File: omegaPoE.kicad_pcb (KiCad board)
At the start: 4 copper layers, 32.4 x 48 mm, 85 parts, among them J1 RJ45-TRANS_POE, J2 CONN_EXPANSION, J3 Conn_02x01, J4 Conn_02x01, Q1 FDM3622, Q2 Q_NMOS_GSD, SW1 SW_Push, T1 PA1276, U1 LM5070, U2 PS2501-1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

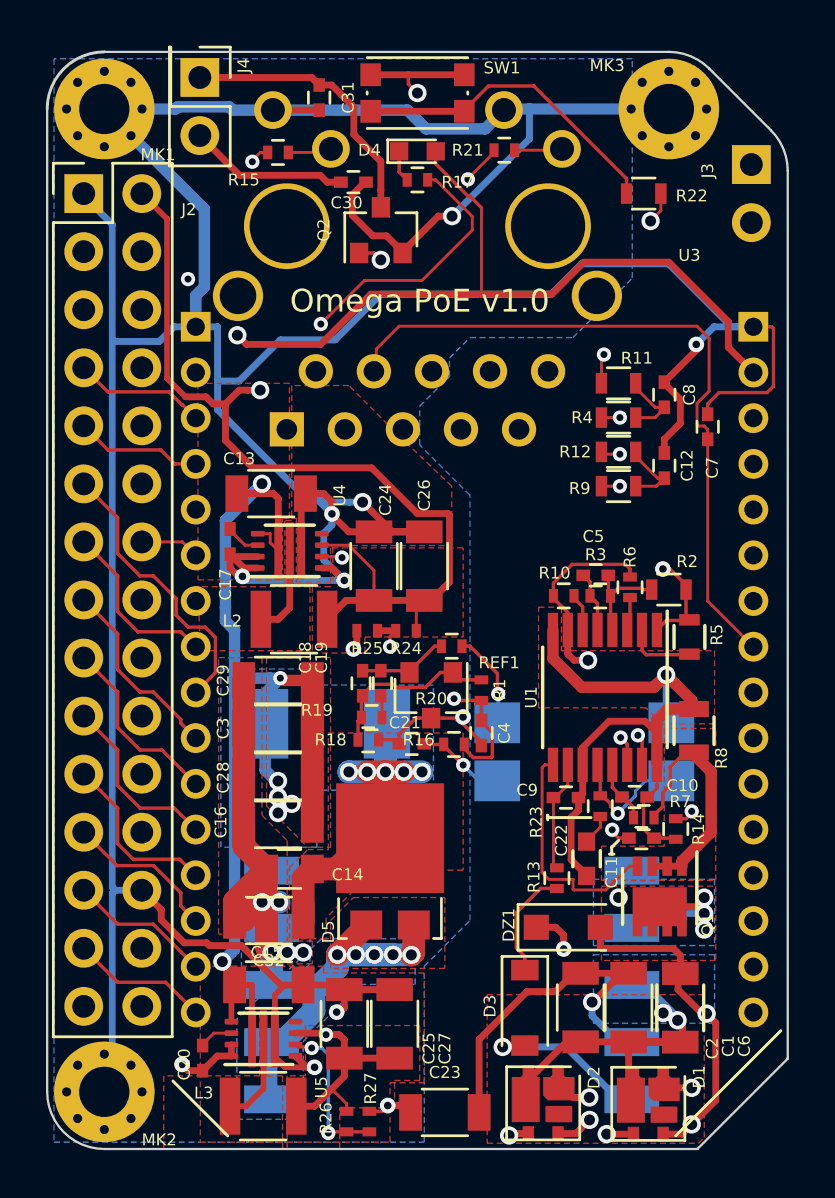
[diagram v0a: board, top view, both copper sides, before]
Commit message: Added rever-semount LED for testing, cleaned up MPN listings some more.
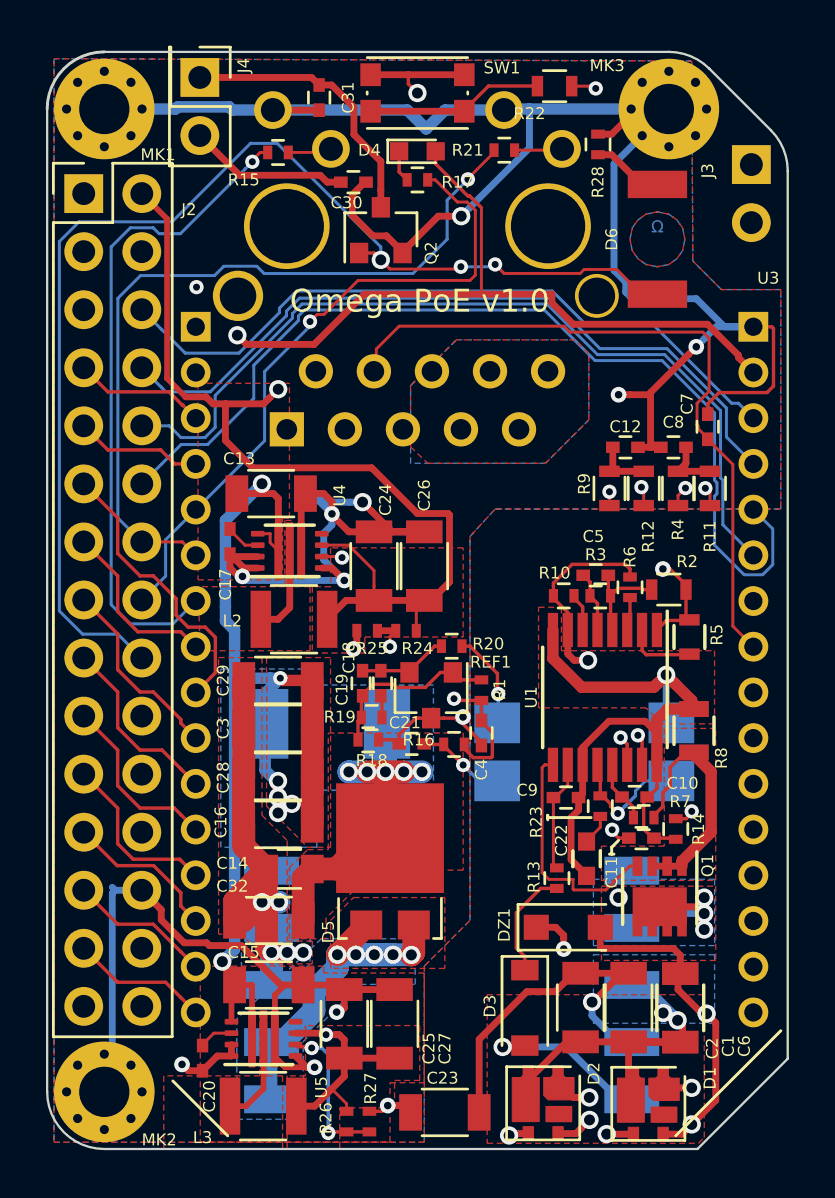
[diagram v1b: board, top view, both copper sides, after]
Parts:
- added D6: LED, lib_fp:LED_reverse_gull, F.Cu at (111.2, 59.7)
- added R28: 100, Resistors_SMD:R_0402, F.Cu at (108.6, 55.5)
- moved R22 6.11 mm to (106.7, 53.0)
- moved R11 6.10 mm to (113.5, 70.6), turned to 90 degrees
- moved R4 4.05 mm to (112.1, 70.6), turned to 270 degrees
- moved C8 2.33 mm to (111.9, 68.8), turned to 180 degrees
- moved R12 1.94 mm to (110.6, 70.6), turned to 90 degrees
- moved C12 1.88 mm to (109.8, 68.8), turned to 0 degrees
- moved R9 0.41 mm to (109.1, 70.6), turned to 270 degrees
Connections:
- J2 pad 5: (no net) -> Net-(J2-Pad5)
- U4 pad 7: Net-(U4-Pad7) -> (no net)
- U5 pad 7: Net-(U5-Pad7) -> (no net)
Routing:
- net GND: track 281.3 -> 218.7 mm, vias 17 -> 18
- net /IO18: track 77.3 -> 88.5 mm, vias 1 -> 3
- net /RESET_BUTTON: track 22.2 -> 30.1 mm
- net Net-(R22-Pad1): track 14.0 -> 7.63 mm
- net /D+: track 36.1 -> 31.1 mm
- net /ETH_TD-: track 33.0 -> 37.1 mm
- net Net-(D6-Pad1): track 0.00 -> 3.14 mm
- net /D-: track 35.6 -> 32.8 mm
- net /ETH_RD-: track 29.3 -> 31.7 mm
- net +5V: track 68.8 -> 70.5 mm
- net +3V3: track 93.2 -> 91.7 mm
- net /IO17: track 27.3 -> 28.8 mm
- net /IO15: track 30.8 -> 29.5 mm
- net +12V: track 92.2 -> 93.2 mm
- net GNDA: track 87.2 -> 88.0 mm
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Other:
- board text added: "v"
- board text added: "Ω"
